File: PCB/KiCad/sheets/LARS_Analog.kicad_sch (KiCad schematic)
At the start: 22 parts, among them U4 OPA2834IDGKR, U5 OPA2834IDGKR

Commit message: add final traces
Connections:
- net SERVO1_OP_IN: now also U5.5 (VIN2+); no longer U5.3 (VIN1+)
- net SERVO1_OP_OUT: now also U5.6 (VIN2-), U5.7 (VOUT2); no longer U5.1 (VOUT1), U5.2 (VIN1-)
- net SERVO2_OP_IN: now also U5.3 (VIN1+); no longer U5.5 (VIN2+)
- net SERVO2_OP_OUT: now also U5.1 (VOUT1), U5.2 (VIN1-); no longer U5.6 (VIN2-), U5.7 (VOUT2)

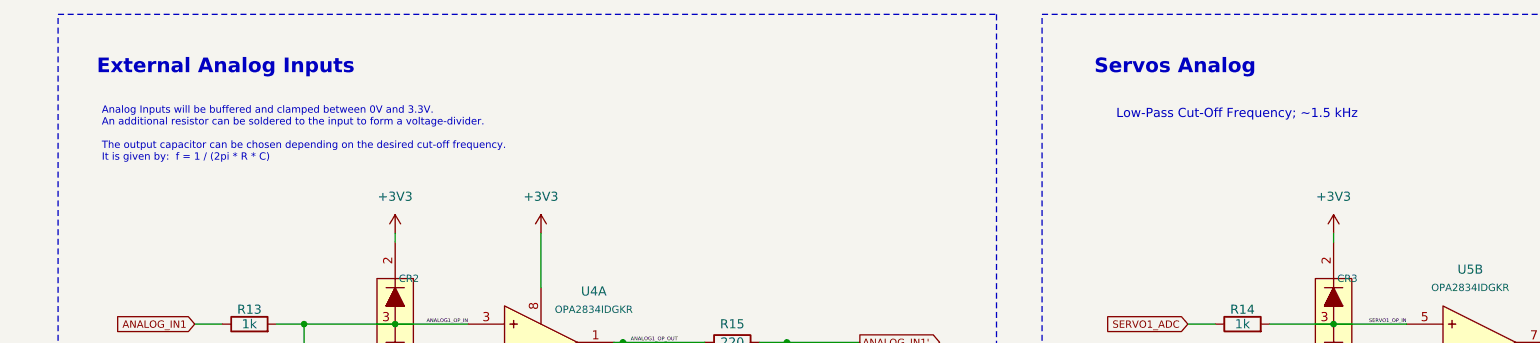
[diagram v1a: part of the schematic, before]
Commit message: change default KiCad schematic font
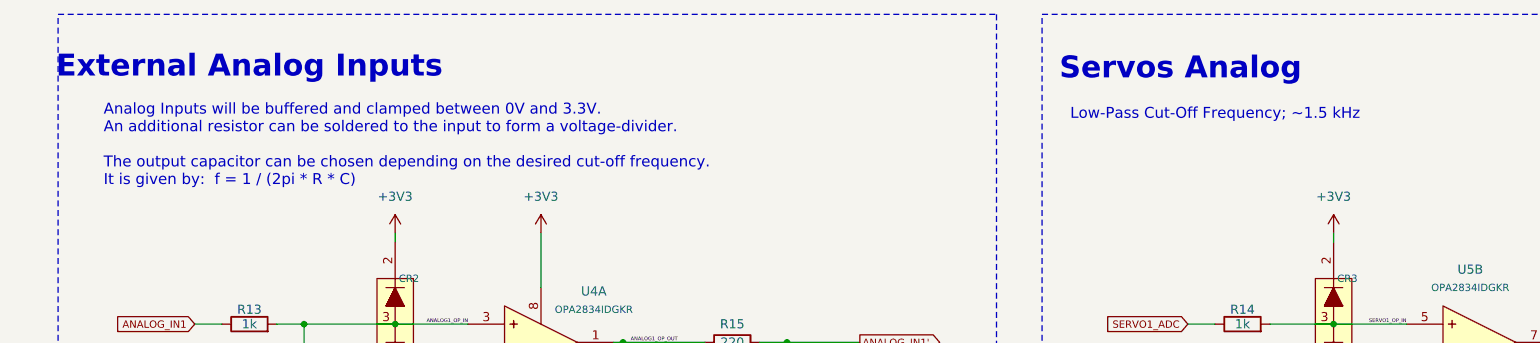
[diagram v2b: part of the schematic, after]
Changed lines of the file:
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@@
 	(text "Servos Analog\n"
 		(exclude_from_sim no)
-		(at 174.752 26.416 0)
+		(at 175.514 26.67 0)
 		(effects
 			(font
-				(size 2.032 2.032)
+				(size 3.048 3.048)
 				(thickness 0.4064)
 				(bold yes)
@@
 	(text "Low-Pass Cut-Off Frequency; ~1.5 kHz"
 		(exclude_from_sim no)
-		(at 183.388 33.02 0)
+		(at 180.34 33.02 0)
 		(effects
 			(font
-				(size 1.27 1.27)
+				(size 1.524 1.524)
 			)
 		)
@@
 	(text "External Analog Inputs\n"
 		(exclude_from_sim no)
-		(at 42.418 26.416 0)
+		(at 45.72 26.416 0)
 		(effects
 			(font
-				(size 2.032 2.032)
+				(size 3.048 3.048)
 				(thickness 0.4064)
 				(bold yes)
@@
 	(text "Analog Inputs will be buffered and clamped between 0V and 3.3V.\nAn additional resistor can be soldered to the input to form a voltage-divider.\n\nThe output capacitor can be chosen depending on the desired cut-off frequency.\nIt is given by:  f = 1 / (2pi * R * C)\n"
 		(exclude_from_sim no)
-		(at 25.146 35.814 0)
+		(at 25.4 37.338 0)
 		(effects
 			(font
-				(size 1.016 1.016)
+				(size 1.524 1.524)
 			)
 			(justify left)

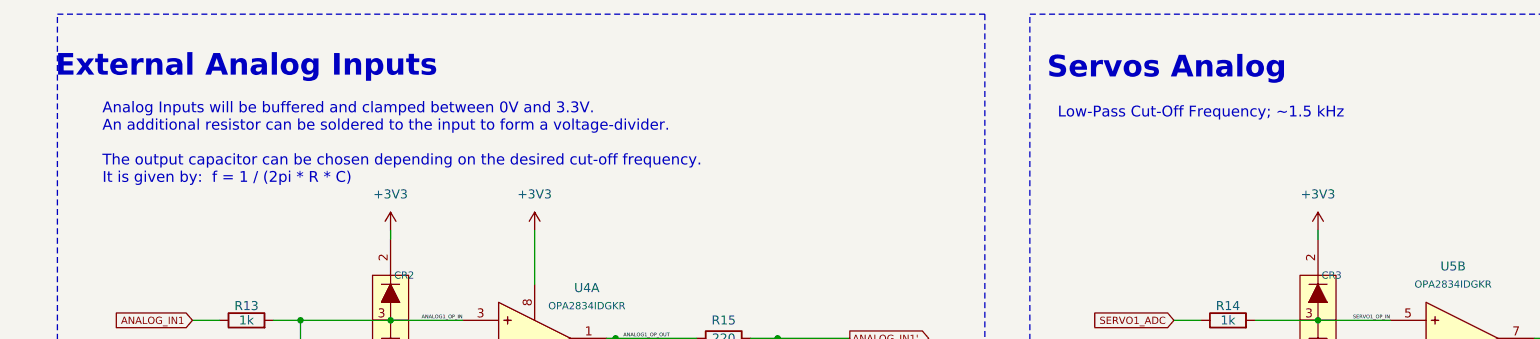
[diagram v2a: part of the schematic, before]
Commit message: update text layout and fix remaining DRC errors
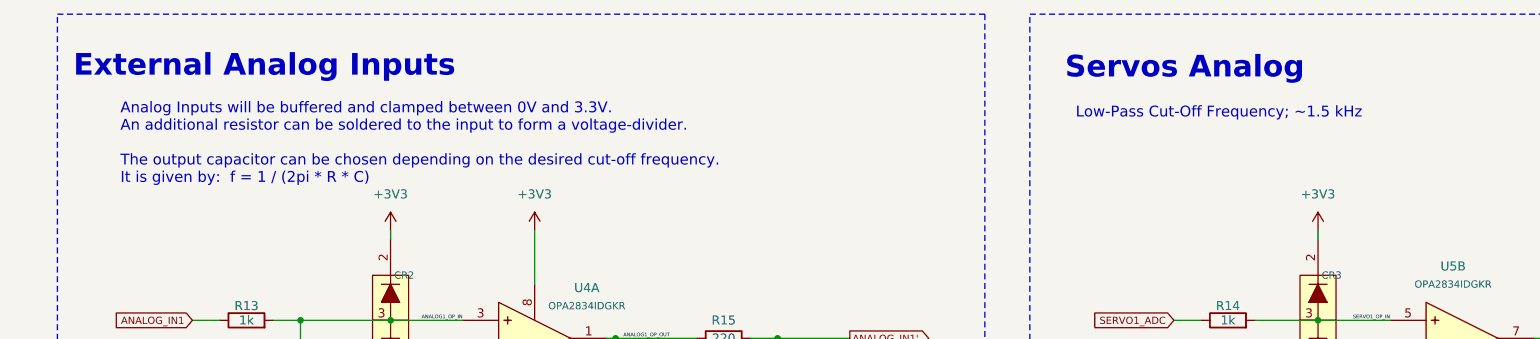
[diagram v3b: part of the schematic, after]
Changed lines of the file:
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@@
 	(text "Servos Analog\n"
 		(exclude_from_sim no)
-		(at 175.514 26.67 0)
+		(at 178.054 26.67 0)
 		(effects
 			(font
@@
 	(text "Low-Pass Cut-Off Frequency; ~1.5 kHz"
 		(exclude_from_sim no)
-		(at 180.34 33.02 0)
+		(at 182.88 33.02 0)
 		(effects
 			(font
@@
 	(text "External Analog Inputs\n"
 		(exclude_from_sim no)
-		(at 45.72 26.416 0)
+		(at 48.26 26.416 0)
 		(effects
 			(font
@@
 	(text "Analog Inputs will be buffered and clamped between 0V and 3.3V.\nAn additional resistor can be soldered to the input to form a voltage-divider.\n\nThe output capacitor can be chosen depending on the desired cut-off frequency.\nIt is given by:  f = 1 / (2pi * R * C)\n"
 		(exclude_from_sim no)
-		(at 25.4 37.338 0)
+		(at 27.94 37.338 0)
 		(effects
 			(font

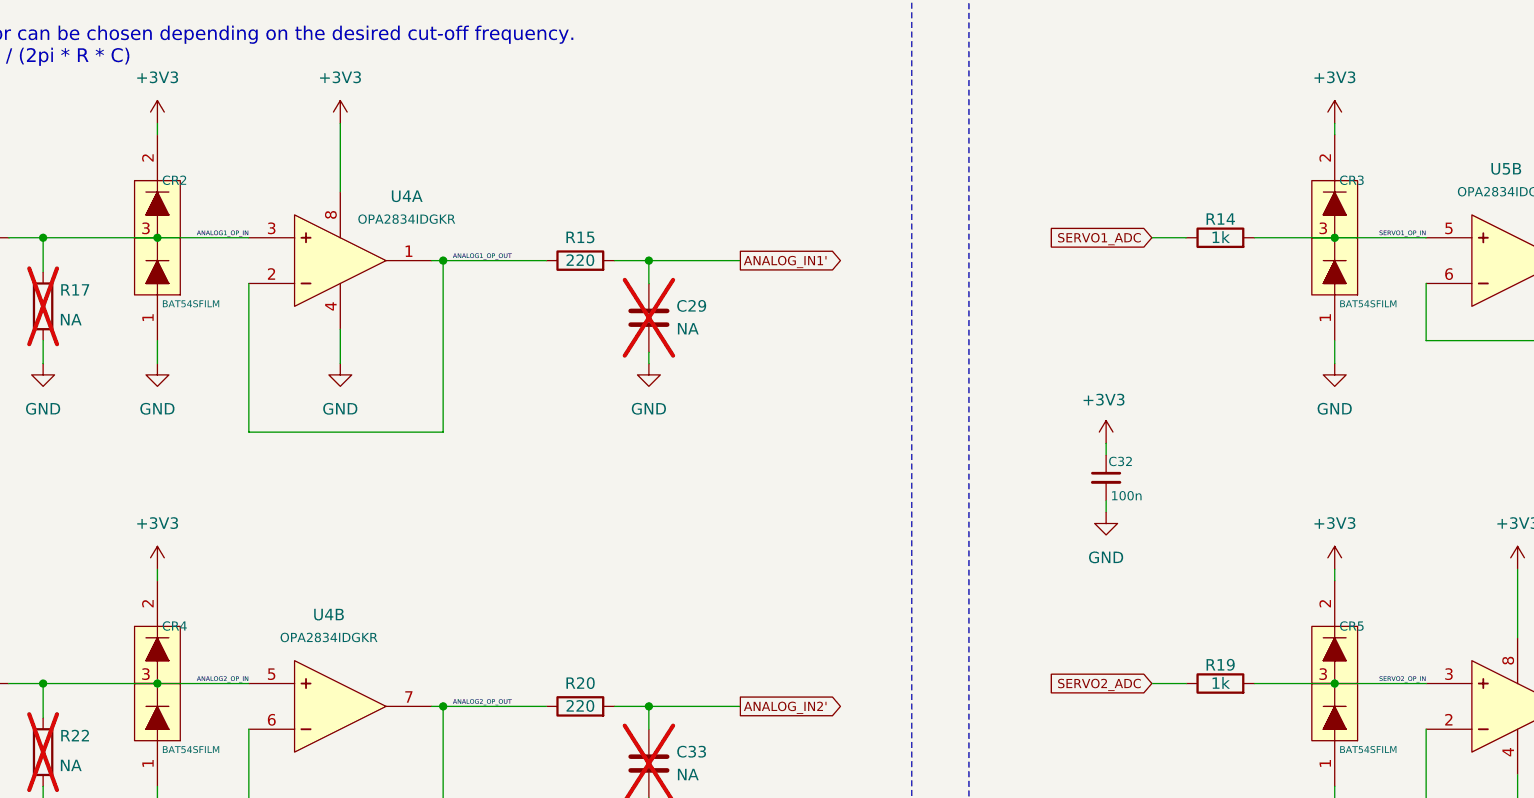
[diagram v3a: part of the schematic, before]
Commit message: add ESD protection and update footprints
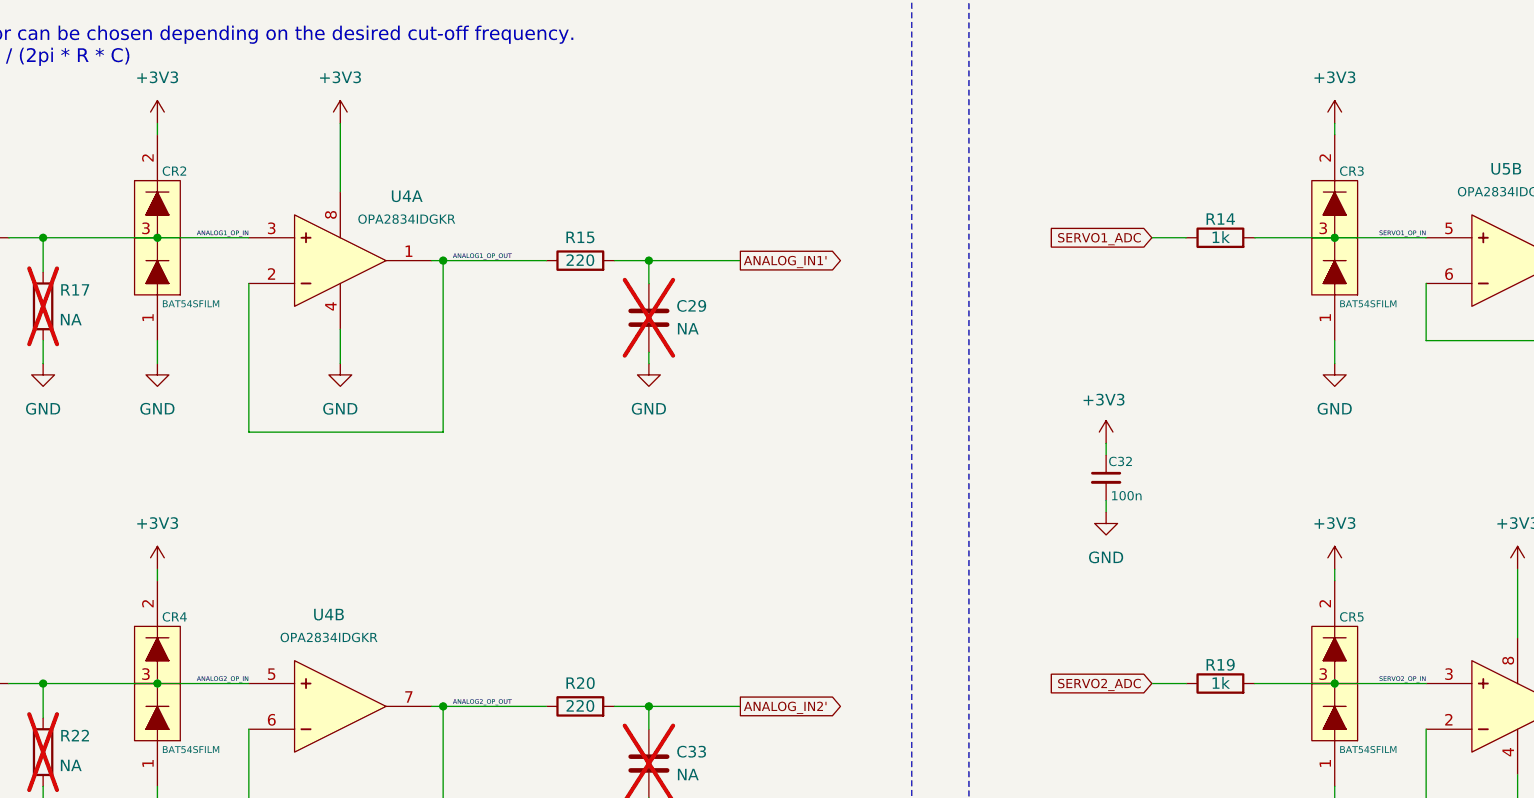
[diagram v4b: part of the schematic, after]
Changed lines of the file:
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@@
 		(dnp no)
 		(fields_autoplaced yes)
-		(property "Reference" "#PWR055"
+		(property "Reference" "#PWR061"
 			(at 196.85 82.55 0)
 			(effects
@@
 			(project "hardware_interface"
 				(path "/ffedf44c-a51a-4124-b6d3-e3f1f256e9ac/81c78436-b6ce-4659-8432-73b82eb5e261"
-					(reference "#PWR055")
+					(reference "#PWR061")
 					(unit 1)
 				)
@@
 		(dnp no)
 		(fields_autoplaced yes)
-		(property "Reference" "#PWR068"
+		(property "Reference" "#PWR075"
 			(at 248.92 132.08 0)
 			(effects
@@
 			(project "hardware_interface"
 				(path "/ffedf44c-a51a-4124-b6d3-e3f1f256e9ac/81c78436-b6ce-4659-8432-73b82eb5e261"
-					(reference "#PWR068")
+					(reference "#PWR075")
 					(unit 1)
 				)
@@
 		(dnp no)
 		(fields_autoplaced yes)
-		(property "Reference" "#PWR048"
+		(property "Reference" "#PWR055"
 			(at 86.36 53.34 0)
 			(effects
@@
 			(project "hardware_interface"
 				(path "/ffedf44c-a51a-4124-b6d3-e3f1f256e9ac/81c78436-b6ce-4659-8432-73b82eb5e261"
-					(reference "#PWR048")
+					(reference "#PWR055")
 					(unit 1)
 				)
@@
 		(dnp no)
 		(fields_autoplaced yes)
-		(property "Reference" "#PWR067"
+		(property "Reference" "#PWR073"
 			(at 196.85 132.08 0)
 			(effects
@@
 			(project "hardware_interface"
 				(path "/ffedf44c-a51a-4124-b6d3-e3f1f256e9ac/81c78436-b6ce-4659-8432-73b82eb5e261"
-					(reference "#PWR067")
+					(reference "#PWR073")
 					(unit 1)
 				)
@@
 		(on_board yes)
 		(dnp no)
-		(property "Reference" "#PWR059"
+		(property "Reference" "#PWR064"
 			(at 171.45 88.9 0)
 			(effects
@@
 			(project "hardware_interface"
 				(path "/ffedf44c-a51a-4124-b6d3-e3f1f256e9ac/81c78436-b6ce-4659-8432-73b82eb5e261"
-					(reference "#PWR059")
+					(reference "#PWR064")
 					(unit 1)
 				)
@@
 		(dnp no)
 		(fields_autoplaced yes)
-		(property "Reference" "#PWR064"
+		(property "Reference" "#PWR070"
 			(at 53.34 132.08 0)
 			(effects
@@
 			(project "hardware_interface"
 				(path "/ffedf44c-a51a-4124-b6d3-e3f1f256e9ac/81c78436-b6ce-4659-8432-73b82eb5e261"
-					(reference "#PWR064")
+					(reference "#PWR070")
 					(unit 1)
 				)
@@
 		(dnp no)
 		(fields_autoplaced yes)
-		(property "Reference" "#PWR062"
+		(property "Reference" "#PWR067"
 			(at 66.04 102.87 0)
 			(effects
@@
 			(project "hardware_interface"
 				(path "/ffedf44c-a51a-4124-b6d3-e3f1f256e9ac/81c78436-b6ce-4659-8432-73b82eb5e261"
-					(reference "#PWR062")
+					(reference "#PWR067")
 					(unit 1)
 				)
@@
 		(dnp no)
 		(fields_autoplaced yes)
-		(property "Reference" "#PWR066"
+		(property "Reference" "#PWR072"
 			(at 120.65 132.08 0)
 			(effects
@@
 			(project "hardware_interface"
 				(path "/ffedf44c-a51a-4124-b6d3-e3f1f256e9ac/81c78436-b6ce-4659-8432-73b82eb5e261"
-					(reference "#PWR066")
+					(reference "#PWR072")
 					(unit 1)
 				)
@@
 		(dnp no)
 		(property "Reference" "CR2"
-			(at 66.548 55.88 0)
+			(at 66.548 54.864 0)
 			(effects
 				(font
@@
 		(dnp no)
 		(fields_autoplaced yes)
-		(property "Reference" "#PWR047"
+		(property "Reference" "#PWR054"
 			(at 66.04 53.34 0)
 			(effects
@@
 			(project "hardware_interface"
 				(path "/ffedf44c-a51a-4124-b6d3-e3f1f256e9ac/81c78436-b6ce-4659-8432-73b82eb5e261"
-					(reference "#PWR047")
+					(reference "#PWR054")
 					(unit 1)
 				)
@@
 		(dnp no)
 		(fields_autoplaced yes)
-		(property "Reference" "#PWR061"
+		(property "Reference" "#PWR066"
 			(at 171.45 99.06 0)
 			(effects
@@
 			(project "hardware_interface"
 				(path "/ffedf44c-a51a-4124-b6d3-e3f1f256e9ac/81c78436-b6ce-4659-8432-73b82eb5e261"
-					(reference "#PWR061")
+					(reference "#PWR066")
 					(unit 1)
 				)
@@
 		(dnp no)
 		(property "Reference" "CR5"
-			(at 197.358 105.41 0)
+			(at 197.358 104.394 0)
 			(effects
 				(font
@@
 		(dnp no)
 		(property "Reference" "CR4"
-			(at 66.548 105.41 0)
+			(at 66.548 104.394 0)
 			(effects
 				(font
@@
 		(dnp no)
 		(fields_autoplaced yes)
-		(property "Reference" "#PWR057"
+		(property "Reference" "#PWR062"
 			(at 248.92 82.55 0)
 			(effects
@@
 			(project "hardware_interface"
 				(path "/ffedf44c-a51a-4124-b6d3-e3f1f256e9ac/81c78436-b6ce-4659-8432-73b82eb5e261"
-					(reference "#PWR057")
+					(reference "#PWR062")
 					(unit 1)
 				)
@@
 		(dnp no)
 		(fields_autoplaced yes)
-		(property "Reference" "#PWR050"
+		(property "Reference" "#PWR069"
 			(at 217.17 102.87 0)
 			(effects
@@
 			(project "hardware_interface"
 				(path "/ffedf44c-a51a-4124-b6d3-e3f1f256e9ac/81c78436-b6ce-4659-8432-73b82eb5e261"
-					(reference "#PWR050")
+					(reference "#PWR069")
 					(unit 1)
 				)
@@
 		(dnp no)
 		(fields_autoplaced yes)
-		(property "Reference" "#PWR054"
+		(property "Reference" "#PWR060"
 			(at 120.65 82.55 0)
 			(effects
@@
 			(project "hardware_interface"
 				(path "/ffedf44c-a51a-4124-b6d3-e3f1f256e9ac/81c78436-b6ce-4659-8432-73b82eb5e261"
-					(reference "#PWR054")
+					(reference "#PWR060")
 					(unit 1)
 				)
@@
 		(dnp no)
 		(fields_autoplaced yes)
-		(property "Reference" "#PWR065"
+		(property "Reference" "#PWR071"
 			(at 66.04 132.08 0)
 			(effects
@@
 			(project "hardware_interface"
 				(path "/ffedf44c-a51a-4124-b6d3-e3f1f256e9ac/81c78436-b6ce-4659-8432-73b82eb5e261"
-					(reference "#PWR065")
+					(reference "#PWR071")
 					(unit 1)
 				)
@@
 		(dnp no)
 		(fields_autoplaced yes)
-		(property "Reference" "#PWR063"
+		(property "Reference" "#PWR068"
 			(at 196.85 102.87 0)
 			(effects
@@
 			(project "hardware_interface"
 				(path "/ffedf44c-a51a-4124-b6d3-e3f1f256e9ac/81c78436-b6ce-4659-8432-73b82eb5e261"
-					(reference "#PWR063")
+					(reference "#PWR068")
 					(unit 1)
 				)
@@
 		(dnp no)
 		(fields_autoplaced yes)
-		(property "Reference" "#PWR053"
+		(property "Reference" "#PWR059"
 			(at 86.36 82.55 0)
 			(effects
@@
 			(project "hardware_interface"
 				(path "/ffedf44c-a51a-4124-b6d3-e3f1f256e9ac/81c78436-b6ce-4659-8432-73b82eb5e261"
-					(reference "#PWR053")
+					(reference "#PWR059")
 					(unit 1)
 				)
@@
 		(dnp no)
 		(fields_autoplaced yes)
-		(property "Reference" "#PWR056"
+		(property "Reference" "#PWR074"
 			(at 217.17 132.08 0)
 			(effects
@@
 			(project "hardware_interface"
 				(path "/ffedf44c-a51a-4124-b6d3-e3f1f256e9ac/81c78436-b6ce-4659-8432-73b82eb5e261"
-					(reference "#PWR056")
+					(reference "#PWR074")
 					(unit 1)
 				)
@@
 		(dnp no)
 		(fields_autoplaced yes)
-		(property "Reference" "#PWR060"
+		(property "Reference" "#PWR065"
 			(at 33.02 97.79 0)
 			(effects
@@
 			(project "hardware_interface"
 				(path "/ffedf44c-a51a-4124-b6d3-e3f1f256e9ac/81c78436-b6ce-4659-8432-73b82eb5e261"
-					(reference "#PWR060")
+					(reference "#PWR065")
 					(unit 1)
 				)
@@
 		(on_board yes)
 		(dnp no)
-		(property "Reference" "#PWR058"
+		(property "Reference" "#PWR063"
 			(at 33.02 87.63 0)
 			(effects
@@
 			(project "hardware_interface"
 				(path "/ffedf44c-a51a-4124-b6d3-e3f1f256e9ac/81c78436-b6ce-4659-8432-73b82eb5e261"
-					(reference "#PWR058")
+					(reference "#PWR063")
 					(unit 1)
 				)
@@
 		(dnp no)
 		(fields_autoplaced yes)
-		(property "Reference" "#PWR049"
+		(property "Reference" "#PWR056"
 			(at 196.85 53.34 0)
 			(effects
@@
 			(project "hardware_interface"
 				(path "/ffedf44c-a51a-4124-b6d3-e3f1f256e9ac/81c78436-b6ce-4659-8432-73b82eb5e261"
-					(reference "#PWR049")
+					(reference "#PWR056")
 					(unit 1)
 				)
@@
 		(dnp no)
 		(fields_autoplaced yes)
-		(property "Reference" "#PWR051"
+		(property "Reference" "#PWR057"
 			(at 53.34 82.55 0)
 			(effects
@@
 			(project "hardware_interface"
 				(path "/ffedf44c-a51a-4124-b6d3-e3f1f256e9ac/81c78436-b6ce-4659-8432-73b82eb5e261"
-					(reference "#PWR051")
+					(reference "#PWR057")
 					(unit 1)
 				)
@@
 		(dnp no)
 		(property "Reference" "CR3"
-			(at 197.358 55.88 0)
+			(at 197.358 54.864 0)
 			(effects
 				(font
@@
 		(dnp no)
 		(fields_autoplaced yes)
-		(property "Reference" "#PWR052"
+		(property "Reference" "#PWR058"
 			(at 66.04 82.55 0)
 			(effects
@@
 			(project "hardware_interface"
 				(path "/ffedf44c-a51a-4124-b6d3-e3f1f256e9ac/81c78436-b6ce-4659-8432-73b82eb5e261"
-					(reference "#PWR052")
+					(reference "#PWR058")
 					(unit 1)
 				)

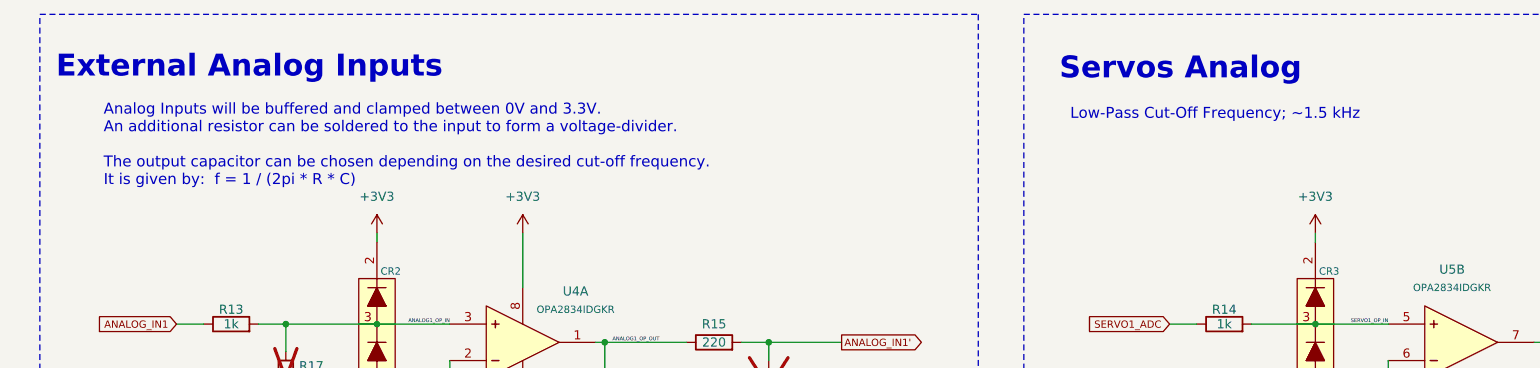
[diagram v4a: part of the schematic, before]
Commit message: PCB: update resistor values and embed font
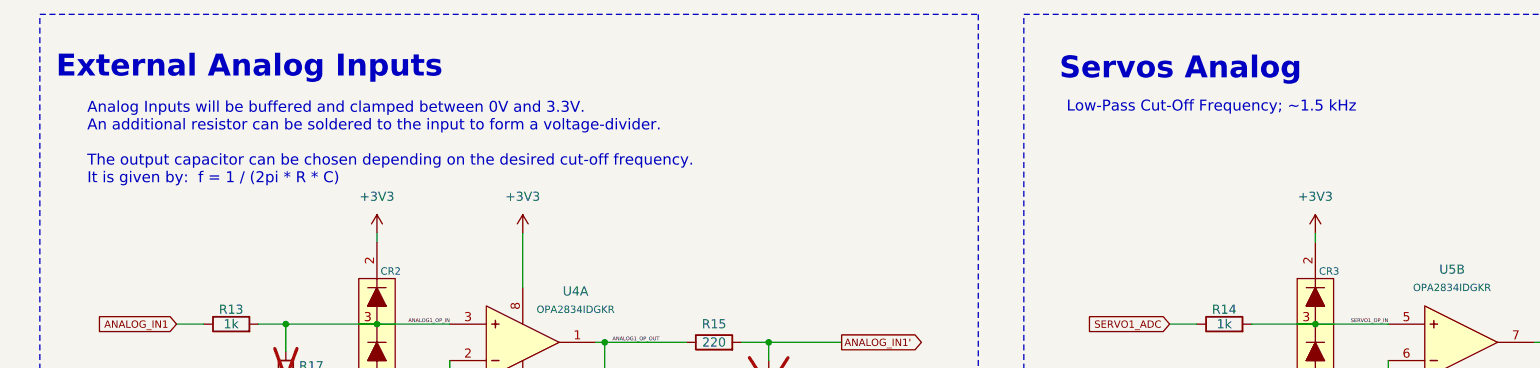
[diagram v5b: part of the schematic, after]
